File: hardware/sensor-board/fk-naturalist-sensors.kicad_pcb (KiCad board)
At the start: 2 copper layers, 20 x 32 mm, 26 parts, among them J1 Conn_01x07, M1 MOUNT_HOLE, M10 FIDUCIAL, M2 MOUNT_HOLE, M3 MOUNT_HOLE, M4 MOUNT_HOLE, M5 FIDUCIAL, M6 FIDUCIAL, M7 FIDUCIAL, M8 FIDUCIAL, M9 FIDUCIAL, U1 MPL3115A2, U2 SHT31, U3 SPH0645, U4 TSL2591

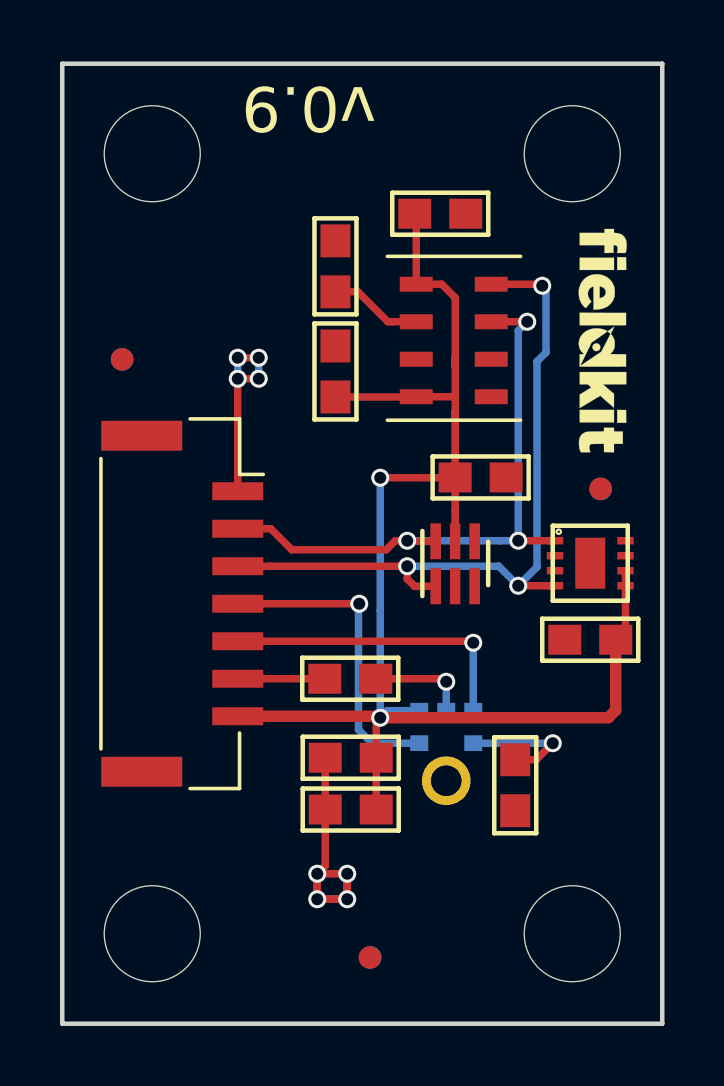
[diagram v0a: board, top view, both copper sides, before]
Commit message: Move to footprints in our library.
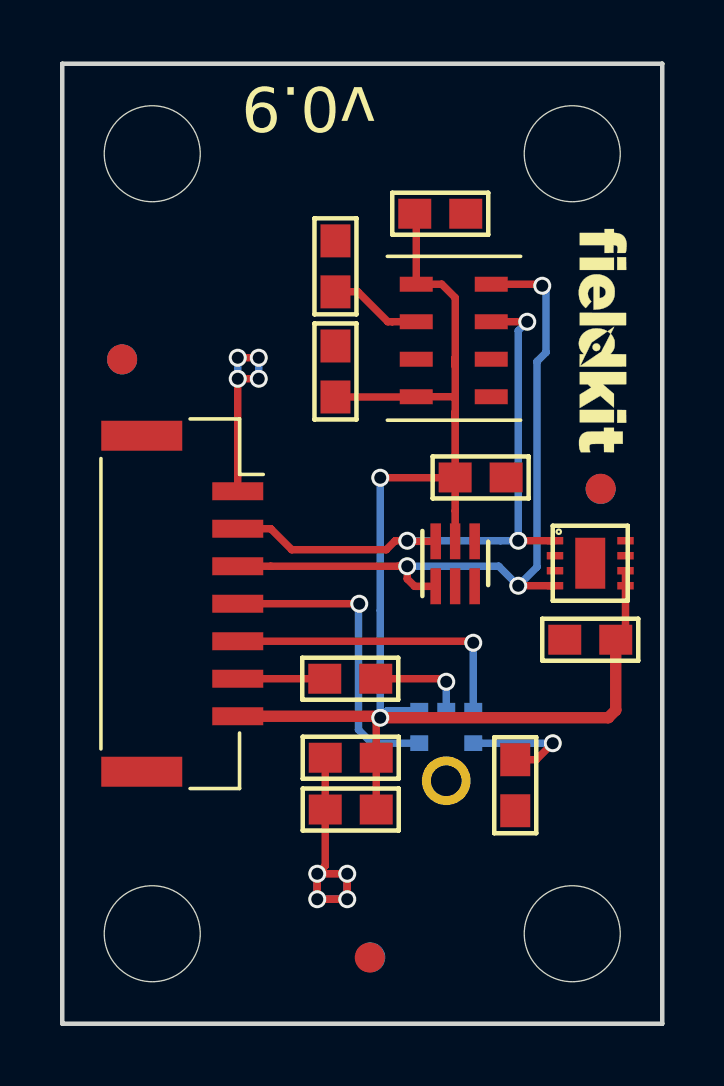
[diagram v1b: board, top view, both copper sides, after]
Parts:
- C1, C2, C3, C4, C5, C6, C7: footprint RocketScreamKicadLibrary:CAP-0603 -> conservify:CAP-0603
- M10, M5, M6, M7, M8, M9: footprint Fiducials:Fiducial_0.75mm_Dia_1.5mm_Outer -> conservify:FIDUCIAL-1MM
- R1, R2: footprint RocketScreamKicadLibrary:RES-0603 -> conservify:RES-0603

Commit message: Add BNO055 to sensor board. Larger connector.
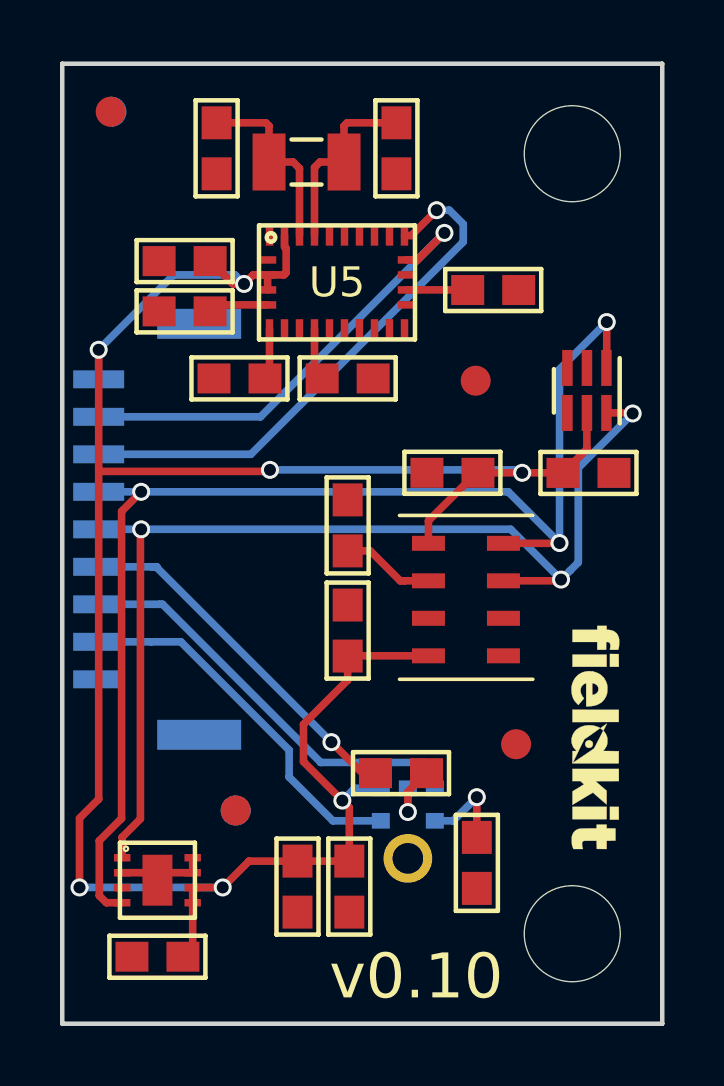
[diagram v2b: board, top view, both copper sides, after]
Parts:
- removed M7, M8: FIDUCIAL, conservify:FIDUCIAL-1MM
- added C10: 100nF, conservify:CAP-0603, F.Cu at (229.5, 110.5)
- added C11: 22pF, conservify:CAP-0603, F.Cu at (231.1, 102.8)
- added C8: 22pF, conservify:CAP-0603, F.Cu at (225.1, 102.8)
- added C9: 100nF, conservify:CAP-0603, F.Cu at (224.1, 106.6)
- added R3: 10K, conservify:RES-0603, F.Cu at (234.4, 107.5)
- added R4: 10K, conservify:RES-0603, F.Cu at (225.9, 110.5)
- added R5: 10K, conservify:RES-0603, F.Cu at (224.1, 108.3)
- added U5: BNO055, conservify:BNO055, F.Cu at (229.2, 107.3)
- added Y1: FC-135, conservify:ABS07, F.Cu at (228.1, 103.3)
- J1: value Conn_01x07 -> CONN_01x09; footprint conservify:Molex_CLIK-Mate_502386-0770_1x07_P1.25mm_Horizontal -> conservify:Molex_CLIK-Mate_502382-0970_1x09_P1.25mm_Vertical; moved to B.Cu
- M1, M2: value MOUNT_HOLE -> FIDUCIAL; footprint conservify:HOLE_NPTH_3.2MM -> conservify:FIDUCIAL-1MM
- moved M5 29.5 mm to (221.6, 101.6)
- moved M2 23.1 mm to (235.1, 122.7)
- moved M1 21.4 mm to (233.8, 110.6)
- moved C2 17.9 mm to (223.2, 129.8)
- moved U2 17.9 mm to (223.2, 127.2)
- moved M6 16.2 mm to (225.8, 124.9)
- moved M10 16.2 mm to (225.8, 124.9)
- moved G*** 13.2 mm to (237.8, 122.5)
- moved C1 8.65 mm to (229.5, 115.4)
- moved C5 8.65 mm to (229.5, 118.9)
- moved C3 8.65 mm to (233.0, 113.6), turned to 180 degrees
- moved U1 8.65 mm to (233.8, 117.9)
- moved M9 8.26 mm to (221.6, 101.6)
- moved U4 7.24 mm to (237.5, 110.9), turned to 270 degrees
- moved C7 4.65 mm to (227.8, 127.4), turned to 270 degrees
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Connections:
- J1 pad 2: /SDA -> /I2S_BCLK
- J1 pad 3: /SCL -> /I2S_WS
- J1 pad 4: /I2S_BCLK -> /I2S_DATA
- J1 pad 5: /I2S_WS -> /SDA
- J1 pad 6: /I2S_DATA -> /SCL
- J1 pad 7: 3V3 -> /SDA2
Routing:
- net 3V3: track 49.4 -> 77.5 mm, vias 2 -> 7
- net /SDA2: track 0.00 -> 18.2 mm, vias 0 -> 1
- net /SCL: track 24.5 -> 42.4 mm
- net /SDA: track 20.6 -> 36.7 mm
- net /SCL2: track 0.00 -> 15.7 mm, vias 0 -> 1
- net GND: track 17.9 -> 3.06 mm, vias 8 -> 0
- net /I2S_DATA: track 2.90 -> 12.2 mm, vias 0 -> 1
- net Net-(C8-Pad1): track 0.00 -> 6.34 mm
- net Net-(C11-Pad1): track 0.00 -> 6.32 mm
- net /I2S_WS: track 10.1 -> 14.0 mm, vias 1 -> 0
- net Net-(R3-Pad1): track 0.00 -> 2.05 mm
- net Net-(R5-Pad1): track 0.00 -> 2.01 mm
- net /I2S_BCLK: track 10.5 -> 12.4 mm, vias 1 -> 0
- net Net-(C10-Pad2): track 0.00 -> 1.74 mm
- net Net-(R4-Pad1): track 0.00 -> 1.70 mm
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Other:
- board text added: "v0.10"
- board text removed: "v0.9"

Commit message: Plot gerbers.
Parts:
- moved G*** 7.85 mm to (230.9, 113.4), turned to 270 degrees
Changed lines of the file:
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@@
     (34 B.Paste user)
     (35 F.Paste user)
-    (36 B.SilkS user hide)
+    (36 B.SilkS user)
     (37 F.SilkS user)
     (38 B.Mask user)
@@
   )
   (setup
-    (last_trace_width 0.254)
+    (last_trace_width 0.25)
     (user_trace_width 0.254)
     (user_trace_width 0.381)
@@
     (visible_elements FFFFFF7F)
     (pcbplotparams
-      (layerselection 0x010fc_80000001)
+      (layerselection 0x010fc_ffffffff)
       (usegerberextensions false)
       (usegerberattributes false)
@@
   )
   (module conservify:conservify_text_negative_4000 (layer B.Cu)
-    (at 223.56064 116.11356 90)
-    (fp_text reference G*** (at 0 0 90) (layer B.SilkS) hide
+    (at 230.9114 113.3602 270)
+    (fp_text reference G*** (at 0 0 270) (layer B.SilkS) hide
       (effects (font (size 1.524 1.524) (thickness 0.3)) (justify mirror))
     )
-    (fp_text value LOGO (at 0.75 0 90) (layer B.SilkS) hide
+    (fp_text value LOGO (at 0.75 0 270) (layer B.SilkS) hide
       (effects (font (size 1.524 1.524) (thickness 0.3)) (justify mirror))
     )
@@
     (at 229.1588 107.2896)
     (descr https://ae-bst.resource.bosch.com/media/products/dokumente/bno055/BST_BNO055_DS000_13.pdf)
-    (fp_text reference U5 (at 0 0) (layer F.SilkS)
+    (fp_text reference U5 (at 0 0) (layer F.SilkS) hide
       (effects (font (size 1 1) (thickness 0.15)))
     )
@@
     (tags "connector Molex CLIK-Mate side entry")
     (attr smd)
-    (fp_text reference J1 (at 0 4.7 90) (layer B.SilkS)
+    (fp_text reference J1 (at 0 4.7 90) (layer B.SilkS) hide
       (effects (font (size 1 1) (thickness 0.15)) (justify mirror))
     )
